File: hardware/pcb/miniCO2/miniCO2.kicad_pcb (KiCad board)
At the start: 4 copper layers, 13.7 x 15.7 mm, 11 parts, among them J1 USB_A, SW1 SW_Push, U1 ATSAMD21E18A-M, U2 AP2112K-3.3, U3 SCD40-D-R2

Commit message: Routing finished
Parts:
- D1, D2: footprint LED_SMD:LED_SK6805_PLCC4_2.4x2.7mm_P1.3mm -> miniCO2:LED_SK6805_PLCC4_2.4x2.7mm_P1.3mm
- U1: footprint Package_DFN_QFN:QFN-32-1EP_5x5mm_P0.5mm_EP3.6x3.6mm -> miniCO2:QFN-32-1EP_5x5mm_P0.5mm_EP3.6x3.6mm
- U3: footprint Sensor:Sensirion_SCD4x-1EP_10.1x10.1mm_P1.25mm_EP4.8x4.8mm -> miniCO2:Sensirion_SCD4x-1EP_10.1x10.1mm_P1.25mm_EP4.8x4.8mm
- moved D2 17.0 mm to (141.5, 97.5)
- moved D1 16.9 mm to (141.5, 97.5)
- moved U3 16.1 mm to (141.5, 89.9), turned to 180 degrees
- moved C4 6.28 mm to (146.6, 87.0), turned to -90 degrees
- moved SW1 1.16 mm to (144.6, 91.6), turned to 0 degrees
- moved C3 0.88 mm to (138.2, 92.8)
- moved C1 0.64 mm to (137.9, 84.7), turned to 0 degrees
- moved U1 0.56 mm to (143.0, 87.2), turned to 90 degrees
- moved C2 0.22 mm to (137.7, 91.6)
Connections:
- U1 pad 19: unconnected-(U1-PA18-Pad19) -> DIN
- U1 pad 31: unconnected-(U1-PA30-Pad31) -> SWCLK
- U1 pad 32: unconnected-(U1-PA31-Pad32) -> SWDIO
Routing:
- net +3.3V: track 0.00 -> 17.4 mm, vias 0 -> 4
- net GND: track 0.00 -> 17.2 mm, vias 0 -> 3
- net DIN: track 0.00 -> 14.2 mm, vias 0 -> 2
- net Net-(U1-~{RESET}): track 0.00 -> 9.09 mm, vias 0 -> 2
- net VBUS: track 0.00 -> 7.53 mm
- net D-: track 0.00 -> 4.71 mm, vias 0 -> 1
- net D+: track 0.00 -> 3.33 mm, vias 0 -> 1
- net SDA: track 0.00 -> 3.12 mm, vias 0 -> 1
- net SCL: track 0.00 -> 2.67 mm, vias 0 -> 1
- net Net-(D1-DOUT): track 0.00 -> 1.31 mm, vias 0 -> 1
- net Net-(U1-VDDCORE): track 0.00 -> 1.20 mm
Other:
- board size 13.7 x 15.7 mm -> 13.7 x 19.8 mm

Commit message: Make prototype
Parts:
- added J2: Conn_01x04_Socket, Connector_PinHeader_1.00mm:PinHeader_1x04_P1.00mm_Vertical, F.Cu at (147.6, 86.2)
- D1, U3: moved to B.Cu
- J1: footprint Connector_USB:917-P81A102ED60200 -> miniCO2:917-P81A102ED60200; moved to B.Cu
- SW1: footprint Button_Switch_SMD:LS75C2D-T -> miniCO2:LS75C2D-T
- moved U3 11.6 mm to (141.5, 101.5), turned to 0 degrees
- moved D2 5.67 mm to (146.2, 94.4)
- moved D1 3.23 mm to (142.1, 94.4), turned to 180 degrees
- moved C1 0.76 mm to (137.2, 84.7), turned to 180 degrees
- turned J1 to 180 degrees
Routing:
- net SCL: track 2.67 -> 19.1 mm, vias 1 -> 2
- net SDA: track 3.12 -> 17.8 mm, vias 1 -> 2
- net VBUS: track 7.53 -> 21.1 mm
- net GND: track 17.2 -> 4.38 mm, vias 3 -> 2
- net SWCLK: track 0.00 -> 10.3 mm, vias 0 -> 1
- net SWDIO: track 0.00 -> 8.59 mm, vias 0 -> 1
- net +3.3V: track 17.4 -> 20.4 mm, vias 4 -> 7
- net D+: track 3.33 -> 5.66 mm
- net D-: track 4.71 -> 2.74 mm
- net Net-(U1-~{RESET}): track 9.09 -> 10.8 mm
- net DIN: track 14.2 -> 12.5 mm
- net Net-(D1-DOUT): track 1.31 -> 2.58 mm, vias 1 -> 0
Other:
- board size 13.7 x 19.8 mm -> 13.7 x 28.2 mm

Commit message: Version 1 finished
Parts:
- D1: footprint miniCO2:LED_SK6805_PLCC4_2.4x2.7mm_P1.3mm -> MiniCO2:LED_SK6805_PLCC4_2.4x2.7mm_P1.3mm
- D2: footprint miniCO2:LED_SK6805_PLCC4_2.4x2.7mm_P1.3mm -> MiniCO2:LED_SK6805_PLCC4_2.4x2.7mm_P1.3mm; moved to F.Cu
- J1: footprint miniCO2:917-P81A102ED60200 -> MiniCO2:917-P81A102ED60200; moved to F.Cu
- J2: footprint Connector_PinHeader_1.00mm:PinHeader_1x04_P1.00mm_Vertical -> MiniCO2:SWD_pogo_pads; moved to B.Cu
- SW1: footprint miniCO2:LS75C2D-T -> MiniCO2:LS75C2D-T
- U1: footprint miniCO2:QFN-32-1EP_5x5mm_P0.5mm_EP3.6x3.6mm -> MiniCO2:QFN-32-1EP_5x5mm_P0.5mm_EP3.6x3.6mm
- U3: footprint miniCO2:Sensirion_SCD4x-1EP_10.1x10.1mm_P1.25mm_EP4.8x4.8mm -> MiniCO2:Sensirion_SCD4x-1EP_10.1x10.1mm_P1.25mm_EP4.8x4.8mm; moved to F.Cu
- moved U3 12.4 mm to (141.5, 89.2), turned to 90 degrees
- moved SW1 9.96 mm to (136.9, 85.2)
- moved J2 6.36 mm to (147.3, 92.6), turned to 0 degrees
- moved C4 6.35 mm to (142.4, 91.8), turned to 180 degrees
- moved D2 5.16 mm to (141.5, 96.5), turned to 0 degrees
- moved C1 2.47 mm to (136.7, 87.1)
- moved D1 2.22 mm to (141.5, 96.5)
- moved U2 1.81 mm to (136.9, 89.9)
- moved C2 1.51 mm to (136.7, 92.7)
- moved U1 1.35 mm to (142.1, 88.2), turned to 0 degrees
- moved C3 0.52 mm to (138.7, 93.0), turned to -90 degrees
- turned J1 to 0 degrees
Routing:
- net SDA: track 17.8 -> 1.76 mm, vias 2 -> 1
- net D-: track 2.74 -> 17.7 mm
- net VBUS: track 21.1 -> 6.73 mm
- net SCL: track 19.1 -> 5.83 mm, vias 2 -> 1
- net Net-(U1-~{RESET}): track 10.8 -> 20.4 mm, vias 2 -> 3
- net +3.3V: track 20.4 -> 11.1 mm, vias 7 -> 5
- net D+: track 5.66 -> 14.8 mm
- net GND: track 4.38 -> 10.3 mm, vias 2 -> 3
- net DIN: track 12.5 -> 14.8 mm
- net SWDIO: track 8.59 -> 10.5 mm, vias 1 -> 2
- net SWCLK: track 10.3 -> 11.8 mm, vias 1 -> 2
- net Net-(D1-DOUT): track 2.58 -> 1.30 mm, vias 0 -> 1
- added copper zone on B.Cu, net +3.3V
- added copper zone on B.Cu, net VBUS
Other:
- board size 13.7 x 28.2 mm -> 13.9 x 18.9 mm
- board text added: "3.3"
- board text added: "CLK"
- board text added: "GND"
- board text added: "IO"
- board text added: "MINICO2 V1"

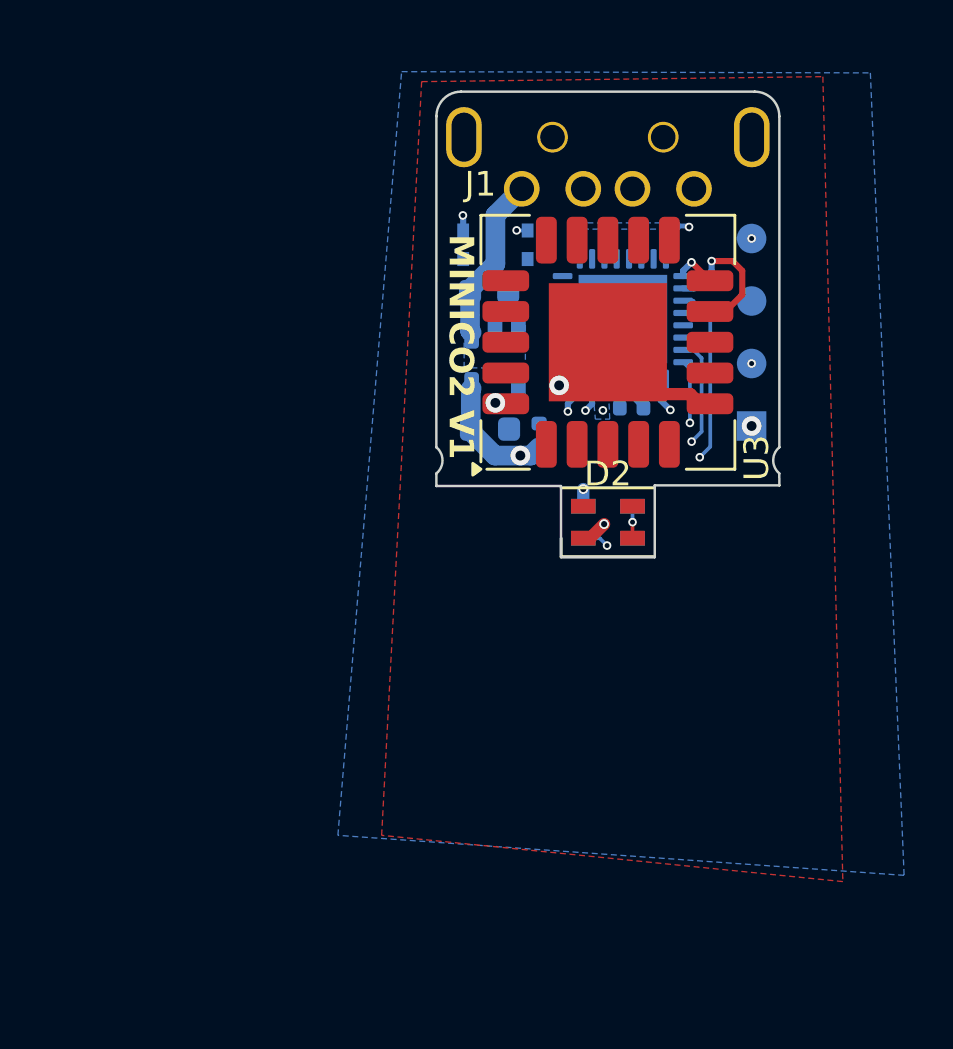
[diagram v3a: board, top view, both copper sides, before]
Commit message: Progress towards single-sided design
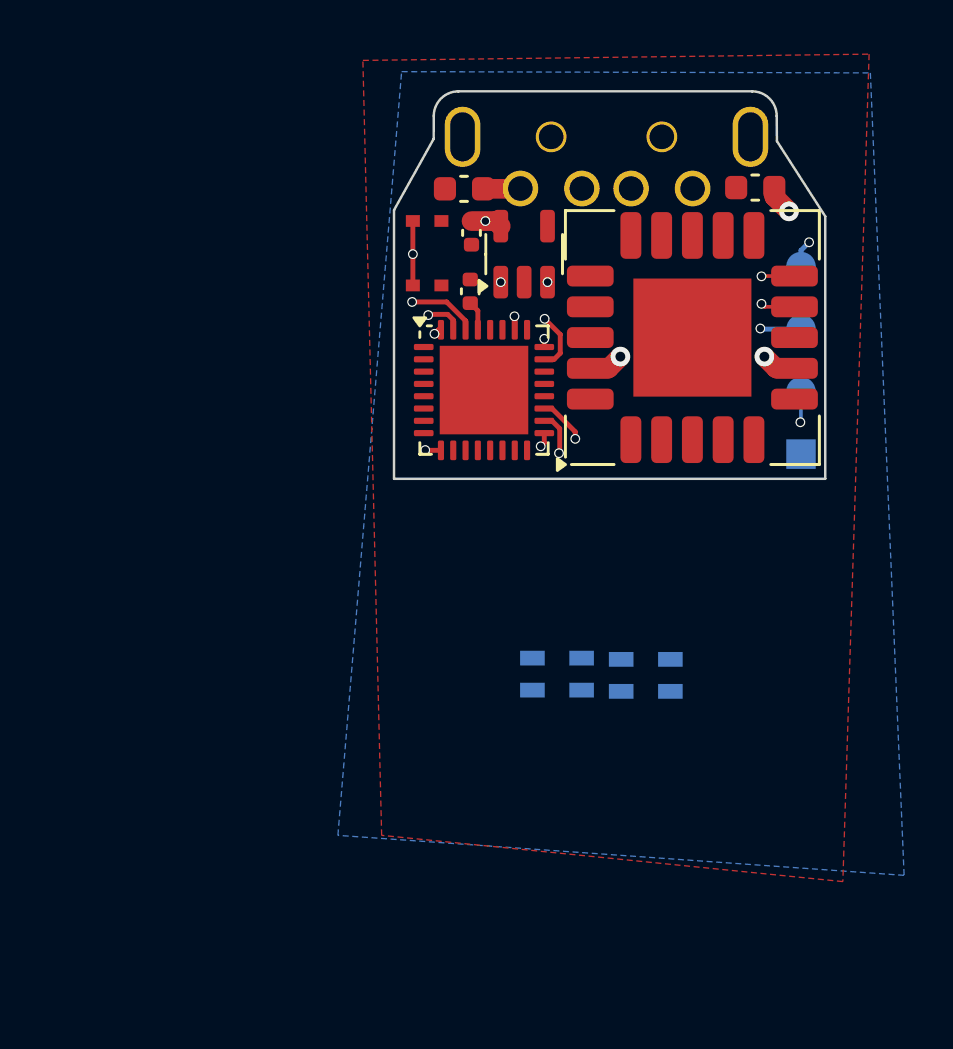
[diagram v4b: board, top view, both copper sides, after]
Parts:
- C1, C2, C3, C4, SW1, U1, U2: moved to F.Cu
- D2: moved to B.Cu
- moved C2 14.6 mm to (147.5, 82.9), turned to 0 degrees
- moved C3 8.68 mm to (135.9, 84.7), turned to 90 degrees
- moved C4 8.09 mm to (135.9, 87.1), turned to -90 degrees
- moved D1 6.51 mm to (139.4, 102.7)
- moved D2 6.41 mm to (143.0, 102.7), turned to 180 degrees
- moved U1 6.34 mm to (136.4, 91.1)
- moved U2 4.48 mm to (138.1, 85.6), turned to 90 degrees
- moved C1 4.30 mm to (135.6, 82.9), turned to 0 degrees
- moved U3 3.44 mm to (144.9, 89.0)
- moved SW1 2.80 mm to (134.1, 85.6), turned to -90 degrees
- moved J2 2.31 mm to (149.3, 93.7)
- moved J1 0.06 mm to (141.4, 80.8)
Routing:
- net DIN: track 14.8 -> 1.93 mm, vias 2 -> 1
- net Net-(U1-~{RESET}): track 20.4 -> 8.35 mm, vias 3 -> 2
- net SDA: track 1.76 -> 13.8 mm, vias 1 -> 2
- net SWCLK: track 11.8 -> 21.5 mm
- net D-: track 17.7 -> 8.34 mm
- net GND: track 10.3 -> 1.66 mm, vias 3 -> 1
- net SCL: track 5.83 -> 14.2 mm, vias 1 -> 2
- net SWDIO: track 10.5 -> 17.9 mm
- net D+: track 14.8 -> 7.90 mm
- net +3.3V: track 11.1 -> 8.97 mm, vias 5 -> 6
- net Net-(D1-DOUT): track 1.30 -> 0.00 mm, vias 1 -> 0
- net VBUS: track 6.73 -> 7.24 mm, vias 0 -> 2
- added copper zone on F.Cu, net GND
- removed copper zone on F.Cu, net +3.3V
- removed copper zone on B.Cu, net GND
- removed copper zone on B.Cu, net VBUS
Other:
- board size 13.9 x 18.9 mm -> 17.5 x 15.7 mm
- board text added: "SWCLK"
- board text added: "SWDIO"
- board text added: "VREF"
- board text removed: "3.3"
- board text removed: "CLK"
- board text removed: "IO"

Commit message: Switch to front facing LEDs
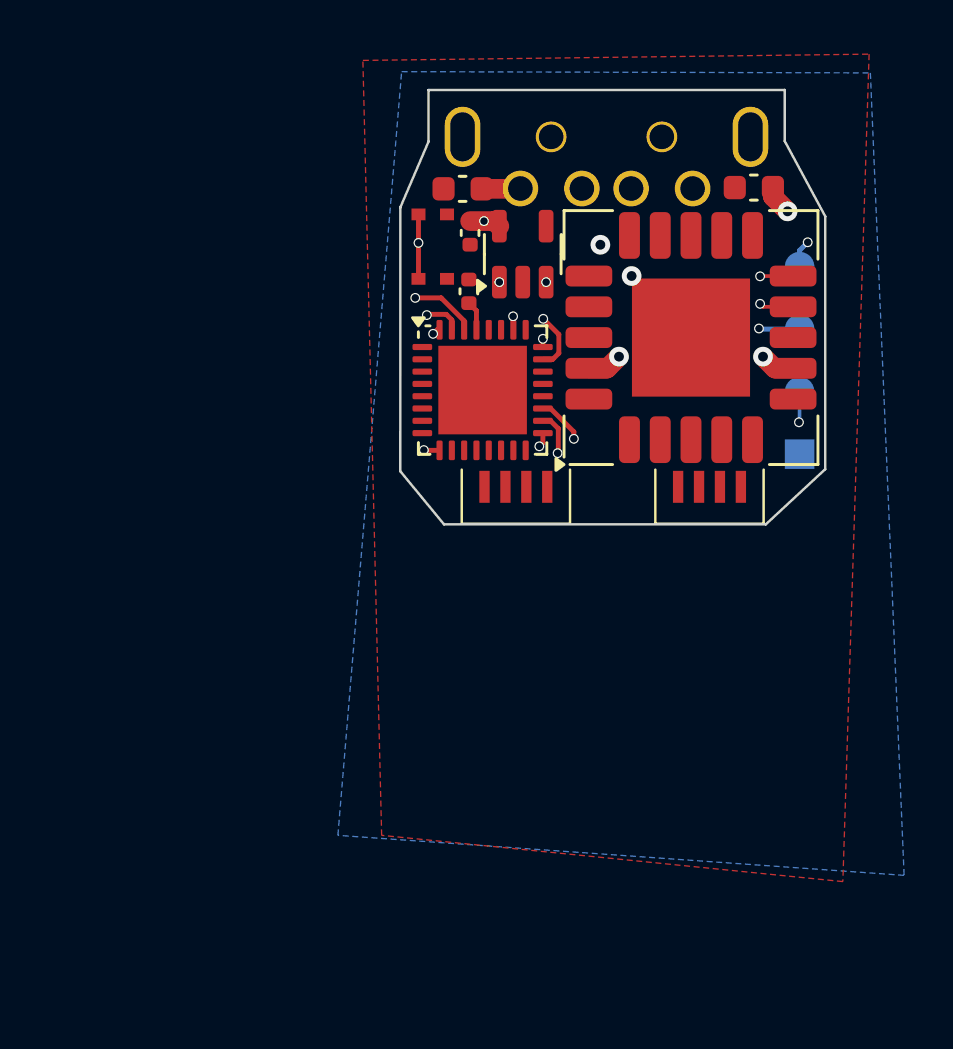
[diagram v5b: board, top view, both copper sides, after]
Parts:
- D1, D2: value SK6805 -> WS2812C-4020; footprint MiniCO2:LED_SK6805_PLCC4_2.4x2.7mm_P1.3mm -> MiniCO2:WS2812C-4020; moved to F.Cu
- moved D2 8.09 mm to (145.6, 95.1)
- moved D1 7.79 mm to (137.7, 95.1)
- moved SW1 0.35 mm to (134.4, 85.3)
- moved C4 0.06 mm to (135.8, 87.1)
- moved J2 0.06 mm to (149.3, 93.7)
- moved U1 0.06 mm to (136.4, 91.1)
- moved U2 0.06 mm to (138.0, 85.6)
- moved U3 0.06 mm to (144.9, 89.0)
- moved C1 0.06 mm to (135.6, 82.9)
- moved C2 0.06 mm to (147.4, 82.9)
- moved C3 0.06 mm to (135.9, 84.7)
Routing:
- net GND: track 1.66 -> 3.46 mm, vias 1 -> 3
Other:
- board size 17.5 x 15.7 mm -> 17.3 x 17.7 mm
- board text added: "MINIC02 V1"

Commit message: Version 1 finished and sent to production
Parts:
- moved D2 7.97 mm to (137.6, 95.0)
- moved D1 7.50 mm to (145.2, 95.0)
- moved J2 0.95 mm to (149.0, 92.8)
- moved C3 0.31 mm to (135.6, 84.7)
- moved C4 0.31 mm to (135.5, 87.1)
- moved U1 0.31 mm to (136.1, 91.1)
- moved U2 0.31 mm to (137.7, 85.6)
- moved U3 0.31 mm to (144.5, 89.0)
- moved C2 0.29 mm to (147.1, 82.9)
- moved C1 0.25 mm to (135.8, 82.9)
- moved SW1 0.22 mm to (134.1, 85.3)
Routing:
- net DIN: track 1.93 -> 11.5 mm, vias 1 -> 2
- net Net-(D1-DOUT): track 0.00 -> 7.28 mm, vias 0 -> 2
- net VBUS: track 7.24 -> 9.44 mm
- net SWCLK: track 21.5 -> 20.1 mm
- net D+: track 7.90 -> 8.74 mm
- net SDA: track 13.8 -> 14.4 mm
- net +3.3V: track 8.86 -> 8.79 mm, vias 6 -> 9
- added copper zone on In1.Cu, net +3.3V
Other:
- board size 17.3 x 17.7 mm -> 17 x 18.5 mm
- board text added: "MINIC02"
- board text removed: "MINIC02 V1"
- board text removed: "MINICO2 V1"
